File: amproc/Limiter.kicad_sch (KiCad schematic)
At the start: 25 parts

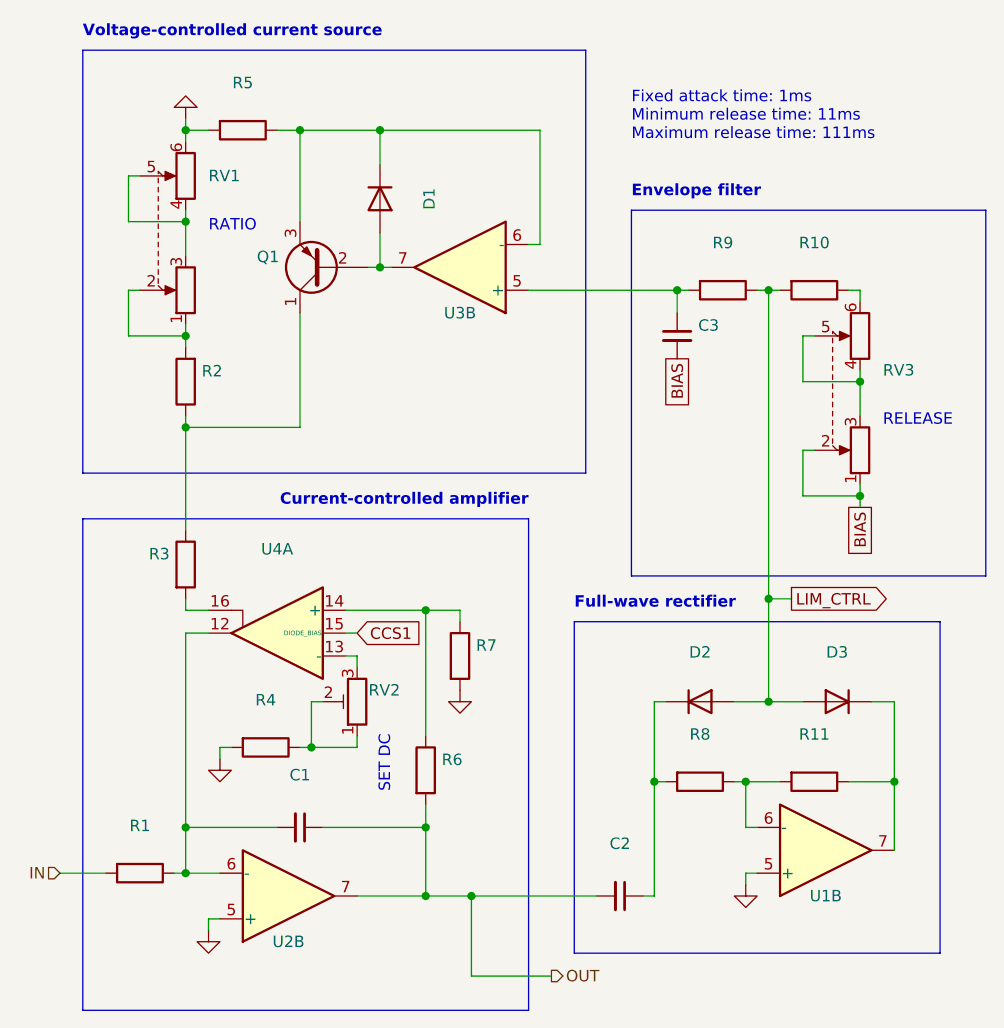
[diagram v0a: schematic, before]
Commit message: Fix U8, U9 pinouts
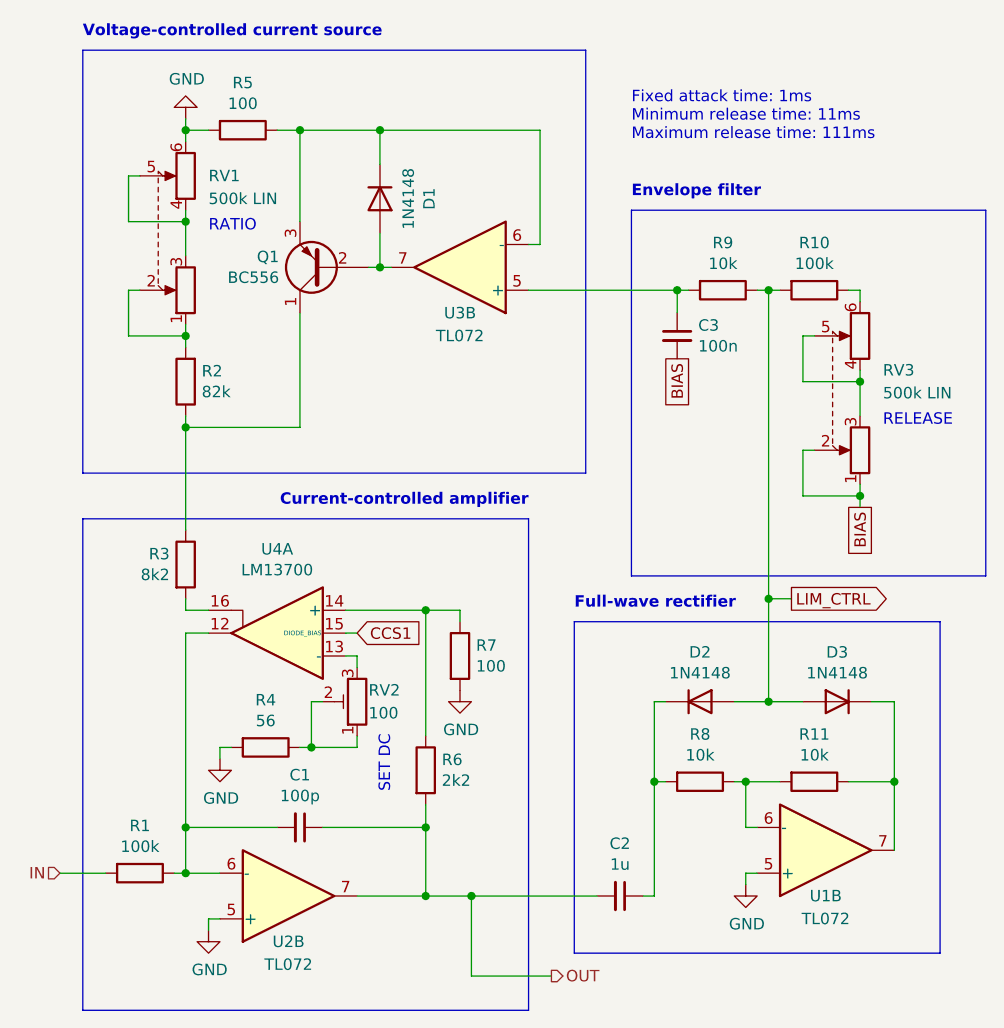
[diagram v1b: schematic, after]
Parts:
- C1: value (none) -> 100p; footprint (none) -> Capacitors_THT:C_Disc_D5.0mm_W2.5mm_P2.50mm
- C2: value (none) -> 1u; footprint (none) -> Capacitors_THT:C_Rect_L7.2mm_W5.5mm_P5.00mm_FKS2_FKP2_MKS2_MKP2
- C3: value (none) -> 100n; footprint (none) -> Capacitors_THT:C_Rect_L7.2mm_W2.5mm_P5.00mm_FKS2_FKP2_MKS2_MKP2
- D1, D2, D3: value (none) -> 1N4148; footprint (none) -> Diodes_THT:D_DO-35_SOD27_P7.62mm_Horizontal
- Q1: value (none) -> BC556; footprint (none) -> TO_SOT_Packages_THT:TO-92_Inline_Narrow_Oval
- R1, R10: value (none) -> 100k; footprint (none) -> amproc:R_Axial_DIN0207_L6.3mm_D2.5mm_P7.62mm_Horizontal_FabText
- R11, R8, R9: value (none) -> 10k; footprint (none) -> amproc:R_Axial_DIN0207_L6.3mm_D2.5mm_P7.62mm_Horizontal_FabText
- R2: value (none) -> 82k; footprint (none) -> amproc:R_Axial_DIN0207_L6.3mm_D2.5mm_P7.62mm_Horizontal_FabText
- R3: value (none) -> 8k2; footprint (none) -> amproc:R_Axial_DIN0207_L6.3mm_D2.5mm_P7.62mm_Horizontal_FabText
- R4: value (none) -> 56; footprint (none) -> amproc:R_Axial_DIN0207_L6.3mm_D2.5mm_P7.62mm_Horizontal_FabText
- R5, R7: value (none) -> 100; footprint (none) -> amproc:R_Axial_DIN0207_L6.3mm_D2.5mm_P7.62mm_Horizontal_FabText
- R6: value (none) -> 2k2; footprint (none) -> amproc:R_Axial_DIN0207_L6.3mm_D2.5mm_P7.62mm_Horizontal_FabText
- RV1, RV3: value (none) -> 500k LIN; footprint (none) -> amproc:PTD902-15K
- RV2: value (none) -> 100; footprint (none) -> amproc:Potentiometer_Trimmer_Bourns_3296W_FabText
- U1, U2, U3: value (none) -> TL072; footprint (none) -> Housings_DIP:DIP-8_W7.62mm_LongPads
- U4: value (none) -> LM13700; footprint (none) -> Housings_DIP:DIP-16_W7.62mm_LongPads

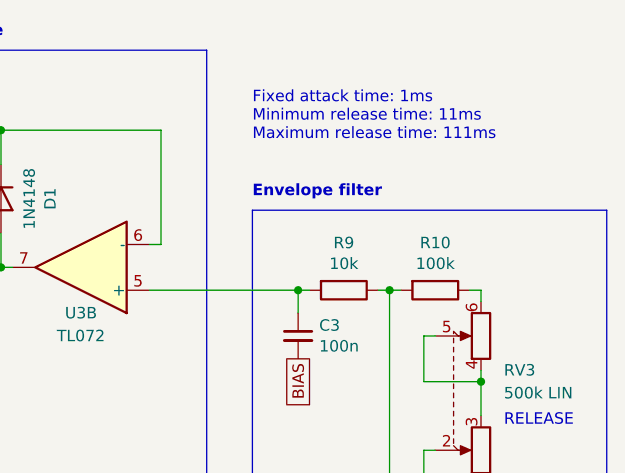
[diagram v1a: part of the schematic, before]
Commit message: Change R10 to 430k to increase minimum release time
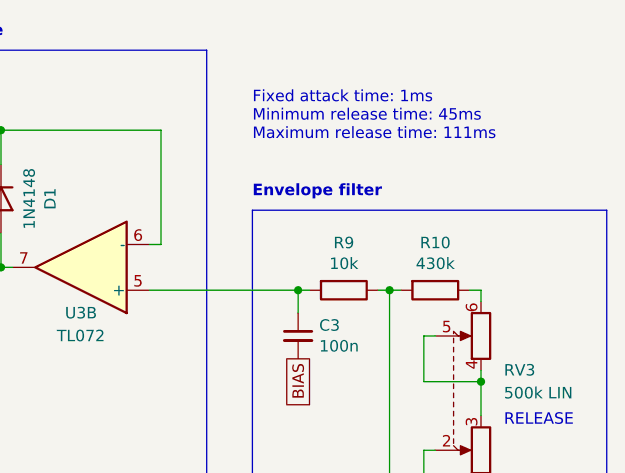
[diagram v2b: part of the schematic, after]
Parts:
- R10: value 100k -> 430k
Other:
- note added: "Fixed attack time: 1ms Minimum release time: 45ms Maximum release time: 111ms"
- note removed: "Fixed attack time: 1ms Minimum release time: 11ms Maximum release time: 111ms"
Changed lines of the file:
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@@
     (effects (font (size 1.27 1.27)) (justify left bottom))
   )
-  (text "Fixed attack time: 1ms\nMinimum release time: 11ms\nMaximum release time: 111ms"
+  (text "Fixed attack time: 1ms\nMinimum release time: 45ms\nMaximum release time: 111ms"
     (at 152.4 49.53 0)
     (effects (font (size 1.27 1.27)) (justify left bottom))
@@
     (in_bom yes) (on_board yes)
     (property "Reference" "R10" (id 0) (at 172.72 60.7822 90))
-    (property "Value" "100k" (id 1) (at 172.72 63.0936 90))
+    (property "Value" "430k" (id 1) (at 172.72 63.0936 90))
     (property "Footprint" "amproc:R_Axial_DIN0207_L6.3mm_D2.5mm_P7.62mm_Horizontal_FabText" (id 2) (at 172.72 64.262 90)
       (effects (font (size 1.27 1.27)) hide)
